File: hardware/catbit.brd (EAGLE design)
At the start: 95 x 72 mm, 37 parts, among them J0 DC24V, Q1 60V/32A/35mΩ, Q2 60V/32A/35mΩ, Q3 60V/32A/35mΩ, Q4 60V/32A/35mΩ, Q5 60V/32A/35mΩ, Q6 60V/32A/35mΩ, Q7 60V/32A/35mΩ, Q8 60V/32A/35mΩ

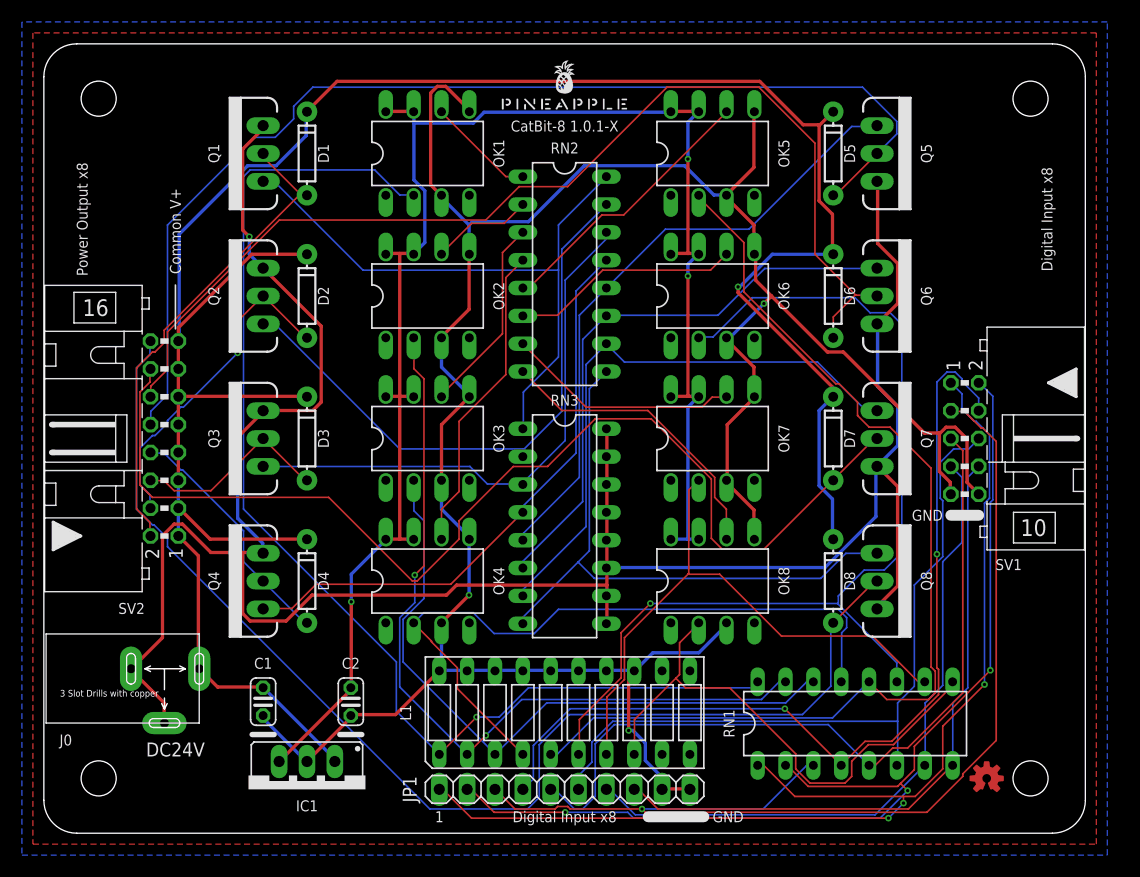
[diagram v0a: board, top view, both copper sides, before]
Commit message: Better power handling.
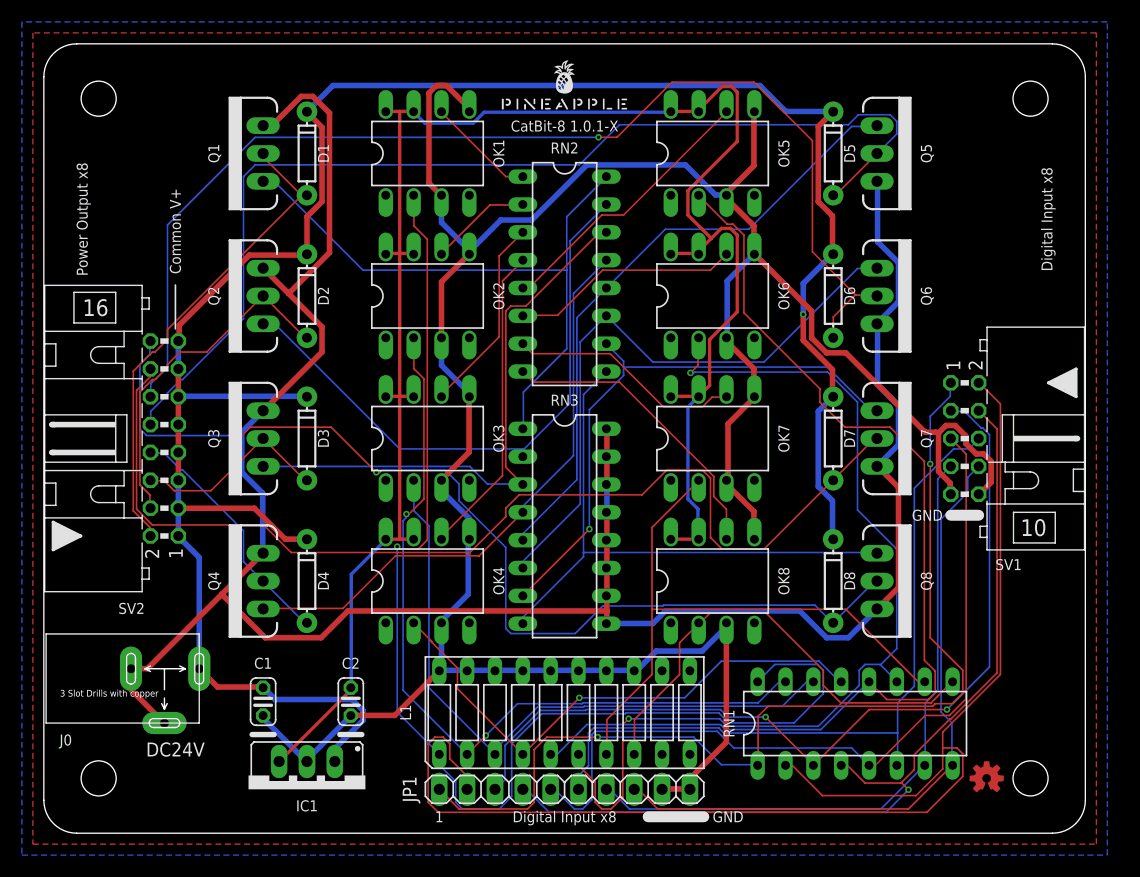
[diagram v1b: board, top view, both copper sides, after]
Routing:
- net D2: track 95.2 -> 122.0 mm, vias 3 -> 0
- net D3: track 99.5 -> 81.4 mm, vias 1 -> 2
- net X8: track 109.9 -> 92.8 mm, vias 0 -> 2
- net VCC: track 148.8 -> 164.1 mm, vias 3 -> 0
- net N$10: track 64.1 -> 49.5 mm, vias 0 -> 1
- net +24V: track 215.6 -> 201.1 mm
- net D1: track 102.2 -> 90.7 mm, vias 3 -> 2
- net GND: track 238.2 -> 248.5 mm, vias 3 -> 0
- net N$22: track 49.3 -> 43.0 mm
- net X6: track 99.1 -> 105.2 mm, vias 0 -> 1
- net GNDA: track 213.1 -> 207.5 mm, vias 2 -> 0
- net X7: track 101.2 -> 96.4 mm
- net X5: track 101.8 -> 97.7 mm
- net N$18: track 52.7 -> 56.1 mm
- net N$16: track 93.0 -> 90.2 mm, vias 1 -> 2
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- added copper zone on layer 1, net +24V
- added copper zone on layer 16, net GNDA
- removed copper zone on layer 1, net GND
- removed copper zone on layer 16, net GND

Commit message: Fixed GND separation.
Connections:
- net GND: no longer C1.2, C2.2, IC1.GND, OK1.5, OK2.5, OK3.5, OK4.5, OK5.5, OK6.5, OK7.5, OK8.5
- net GNDA: now also C1.2, C2.2, IC1.GND, OK1.5, OK2.5, OK3.5, OK4.5, OK5.5, OK6.5, OK7.5, OK8.5
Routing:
- net GNDA: track 207.5 -> 310.2 mm, vias 0 -> 4
- net GND: track 248.5 -> 189.1 mm, vias 0 -> 5
- net +24V: track 201.1 -> 223.6 mm
- net N$1: track 111.4 -> 131.8 mm, vias 1 -> 0
- net X8: track 92.8 -> 110.3 mm, vias 2 -> 0
- net X5: track 97.7 -> 81.8 mm, vias 0 -> 1
- net D2: track 122.0 -> 110.5 mm, vias 0 -> 1
- net X7: track 96.4 -> 104.9 mm
- net X6: track 105.2 -> 100.6 mm, vias 1 -> 0
- net N$16: track 90.2 -> 94.3 mm
- net N$15: track 57.0 -> 60.9 mm
- net N$18: track 56.1 -> 52.7 mm
- net N$19: track 56.1 -> 58.7 mm
- net N$4: track 73.5 -> 76.1 mm
- net VCC: track 164.1 -> 161.6 mm, vias 0 -> 2
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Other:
- board text added: "CatBit-8 1.0.2-X"
- board text removed: "CatBit-8 1.0.1-X"

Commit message: Silk.
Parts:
- RN1: value (none) -> 160
- RN2: value (none) -> 100
- RN3: value (none) -> 1k
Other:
- board text added: "101"
- board text added: "102"
- board text added: "161"
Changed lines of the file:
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@@
 <text x="61" y="1.5" size="1" layer="25" align="center-left">GND</text>
 <text x="82" y="29" size="1" layer="25" align="center-right">GND</text>
+<text x="47.5" y="50" size="1" layer="25" align="bottom-center">101</text>
+<text x="47.5" y="27" size="1" layer="25" align="bottom-center">102</text>
+<text x="75.5" y="10" size="1" layer="25" rot="R90" align="bottom-center">161</text>
 </plain>
 <attributes>
@@
 <attribute name="VALUE" x="31.444" y="61.365" size="1.27" layer="27" ratio="10"/>
 </element>
-<element name="RN1" library="resistor-dil" library_urn="urn:adsk.eagle:library:342" package="DIL16" package3d_urn="urn:adsk.eagle:package:922/2" value="" x="74" y="10" smashed="yes">
+<element name="RN1" library="resistor-dil" library_urn="urn:adsk.eagle:library:342" package="DIL16" package3d_urn="urn:adsk.eagle:package:922/2" value="160" x="74" y="10" smashed="yes">
 <attribute name="MF" value="" x="74" y="10" size="1.778" layer="27" display="off"/>
 <attribute name="MPN" value="" x="74" y="10" size="1.778" layer="27" display="off"/>
@@
 <attribute name="VALUE" x="43.69" y="16.715" size="1.27" layer="27" ratio="10"/>
 </element>
-<element name="RN2" library="resistor-dil" library_urn="urn:adsk.eagle:library:342" package="DIL16" package3d_urn="urn:adsk.eagle:package:922/2" value="" x="47.5" y="51" smashed="yes" rot="R270">
+<element name="RN2" library="resistor-dil" library_urn="urn:adsk.eagle:library:342" package="DIL16" package3d_urn="urn:adsk.eagle:package:922/2" value="100" x="47.5" y="51" smashed="yes" rot="R270">
 <attribute name="MF" value="" x="47.5" y="51" size="1.778" layer="27" rot="R270" display="off"/>
 <attribute name="MPN" value="" x="47.5" y="51" size="1.778" layer="27" rot="R270" display="off"/>
@@
 <attribute name="VALUE" x="46.865" y="58.493" size="1.27" layer="27" ratio="10" rot="R270"/>
 </element>
-<element name="RN3" library="resistor-dil" library_urn="urn:adsk.eagle:library:342" package="DIL16" package3d_urn="urn:adsk.eagle:package:922/2" value="" x="47.5" y="28" smashed="yes" rot="R270">
+<element name="RN3" library="resistor-dil" library_urn="urn:adsk.eagle:library:342" package="DIL16" package3d_urn="urn:adsk.eagle:package:922/2" value="1k" x="47.5" y="28" smashed="yes" rot="R270">
 <attribute name="MF" value="" x="47.5" y="28" size="1.778" layer="27" rot="R270" display="off"/>
 <attribute name="MPN" value="" x="47.5" y="28" size="1.778" layer="27" rot="R270" display="off"/>

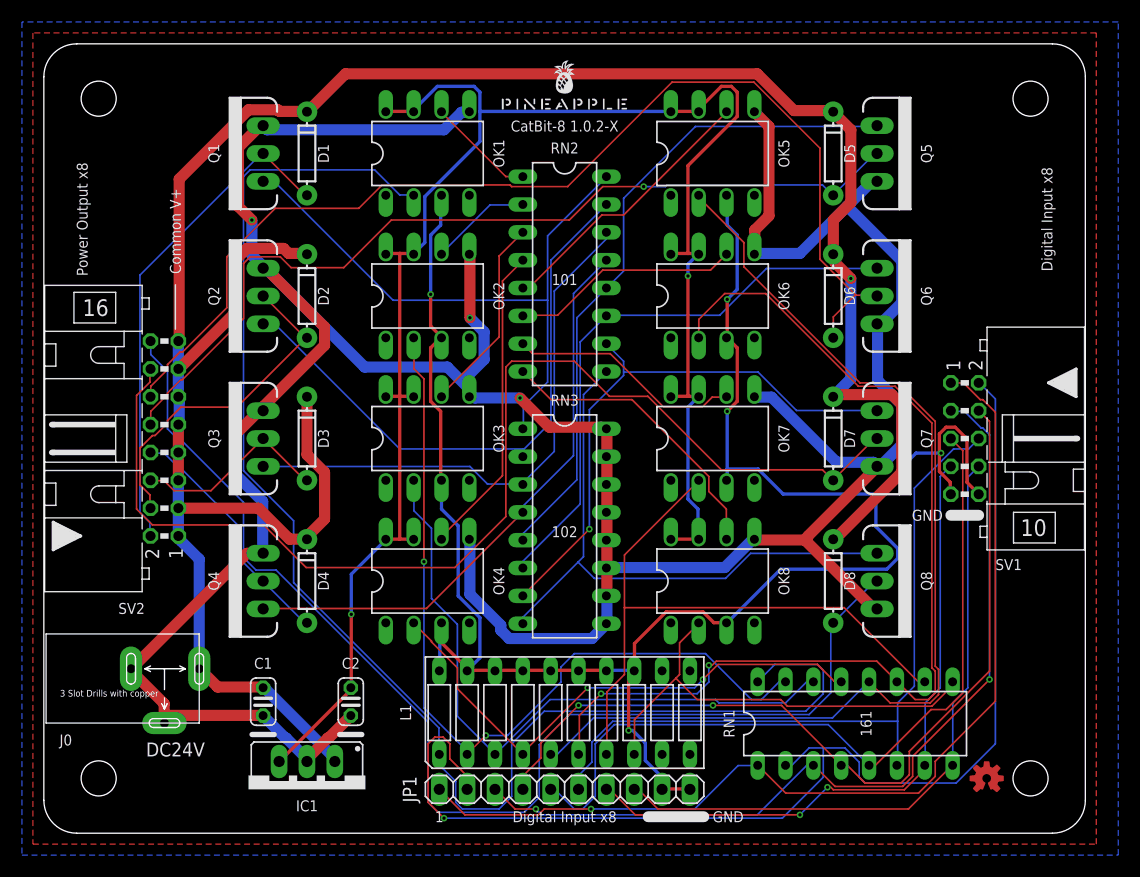
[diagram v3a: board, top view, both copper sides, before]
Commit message: Clean up around OUTPUT port.
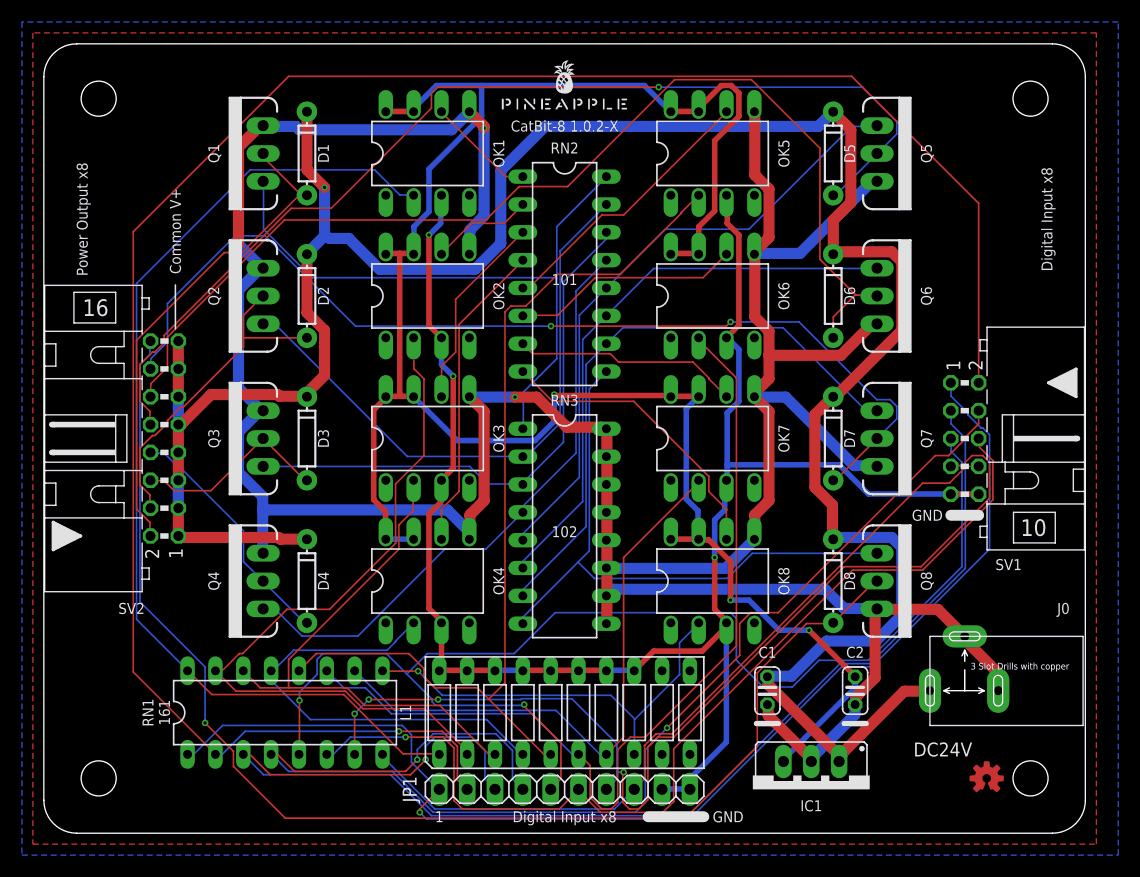
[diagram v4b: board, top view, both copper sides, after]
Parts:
- moved J0 73.0 mm to (84.0, 13.0), turned to 180 degrees
- moved RN1 52.0 mm to (22.0, 11.0)
- moved C1 46.0 mm to (66.0, 13.0)
- moved C2 46.0 mm to (74.0, 13.0)
- moved IC1 46.0 mm to (70.0, 4.00)
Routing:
- net D2: track 110.5 -> 182.7 mm
- net D5: track 72.3 -> 114.7 mm, vias 0 -> 2
- net D3: track 80.6 -> 121.8 mm, vias 2 -> 1
- net N$1: track 131.8 -> 93.9 mm
- net D4: track 79.8 -> 116.4 mm
- net D7: track 60.6 -> 93.6 mm, vias 2 -> 4
- net GND: track 189.1 -> 159.7 mm, vias 5 -> 3
- net VCC: track 161.6 -> 186.7 mm, vias 2 -> 3
- net D6: track 67.2 -> 89.4 mm, vias 0 -> 1
- net D1: track 90.4 -> 109.9 mm
- net X5: track 81.8 -> 97.2 mm
- net X7: track 104.9 -> 91.7 mm, vias 0 -> 2
- net D8: track 59.7 -> 71.3 mm
- net N$16: track 94.3 -> 82.8 mm, vias 2 -> 0
- net N$7: track 60.1 -> 49.8 mm
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- added copper zone on layer 16, net GND
- removed copper zone on layer 16, net GNDA
